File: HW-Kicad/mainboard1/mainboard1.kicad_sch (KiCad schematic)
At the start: 1 part, among them M1 LightAPRS

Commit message: comienzo mainboard
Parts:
- removed M1: LightAPRS, LightAPRS:LightAPRS, symbol LightAPRS:LightAPRS
- added J1: Conn_01x02_Male, Connector_Molex:Molex_KK-254_AE-6410-02A_1x02_P2.54mm_Vertical, symbol Connector:Conn_01x02_Male
- added J2: Conn_01x02_Male, Connector_PinHeader_2.54mm:PinHeader_1x02_P2.54mm_Horizontal, symbol Connector:Conn_01x02_Male
- added J3: Conn_01x07_Male, Connector_PinHeader_2.54mm:PinHeader_1x07_P2.54mm_Horizontal, symbol Connector:Conn_01x07_Male
- added J4, J5: Conn_01x04_Male, Connector_Molex:Molex_KK-254_AE-6410-04A_1x04_P2.54mm_Vertical, symbol Connector:Conn_01x04_Male
- added U1: ESP32-DevKitC, espressif:ESP32-DevKitC, symbol Espressif:ESP32-DevKitC
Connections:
- new net GND: J1.2 (Pin_2), J2.2 (Pin_2), J4.4 (Pin_4), J5.4 (Pin_4), U1.32 (GND), U1.38 (GND)
- new net MISO: J3.6 (Pin_6)
- new net MOSI: J3.7 (Pin_7)
- new net PAYLOAD1RX: J4.2 (Pin_2)
- new net PAYLOAD1TX: J4.3 (Pin_3)
- new net PAYLOAD2RX: J5.2 (Pin_2)
- new net PAYLOAD2TX: J5.3 (Pin_3)
- new net RST: J3.2 (Pin_2)
- new net SCK: J3.5 (Pin_5)
- new net SCL: J3.3 (Pin_3)
- new net SDA: J3.4 (Pin_4)
- new net VBAT: J1.1 (Pin_1), J2.1 (Pin_1), J4.1 (Pin_1), J5.1 (Pin_1), U1.19 (5V)
- no-connect marks 0 -> 1
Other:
- note added: "4,5 to 10v max"
- note added: "7.5V"
- note added: "Battery Module Input"
- note added: "LightAPRS Connector"
- note added: "Payload 1 Connector"
- note added: "Payload 2 Connector"

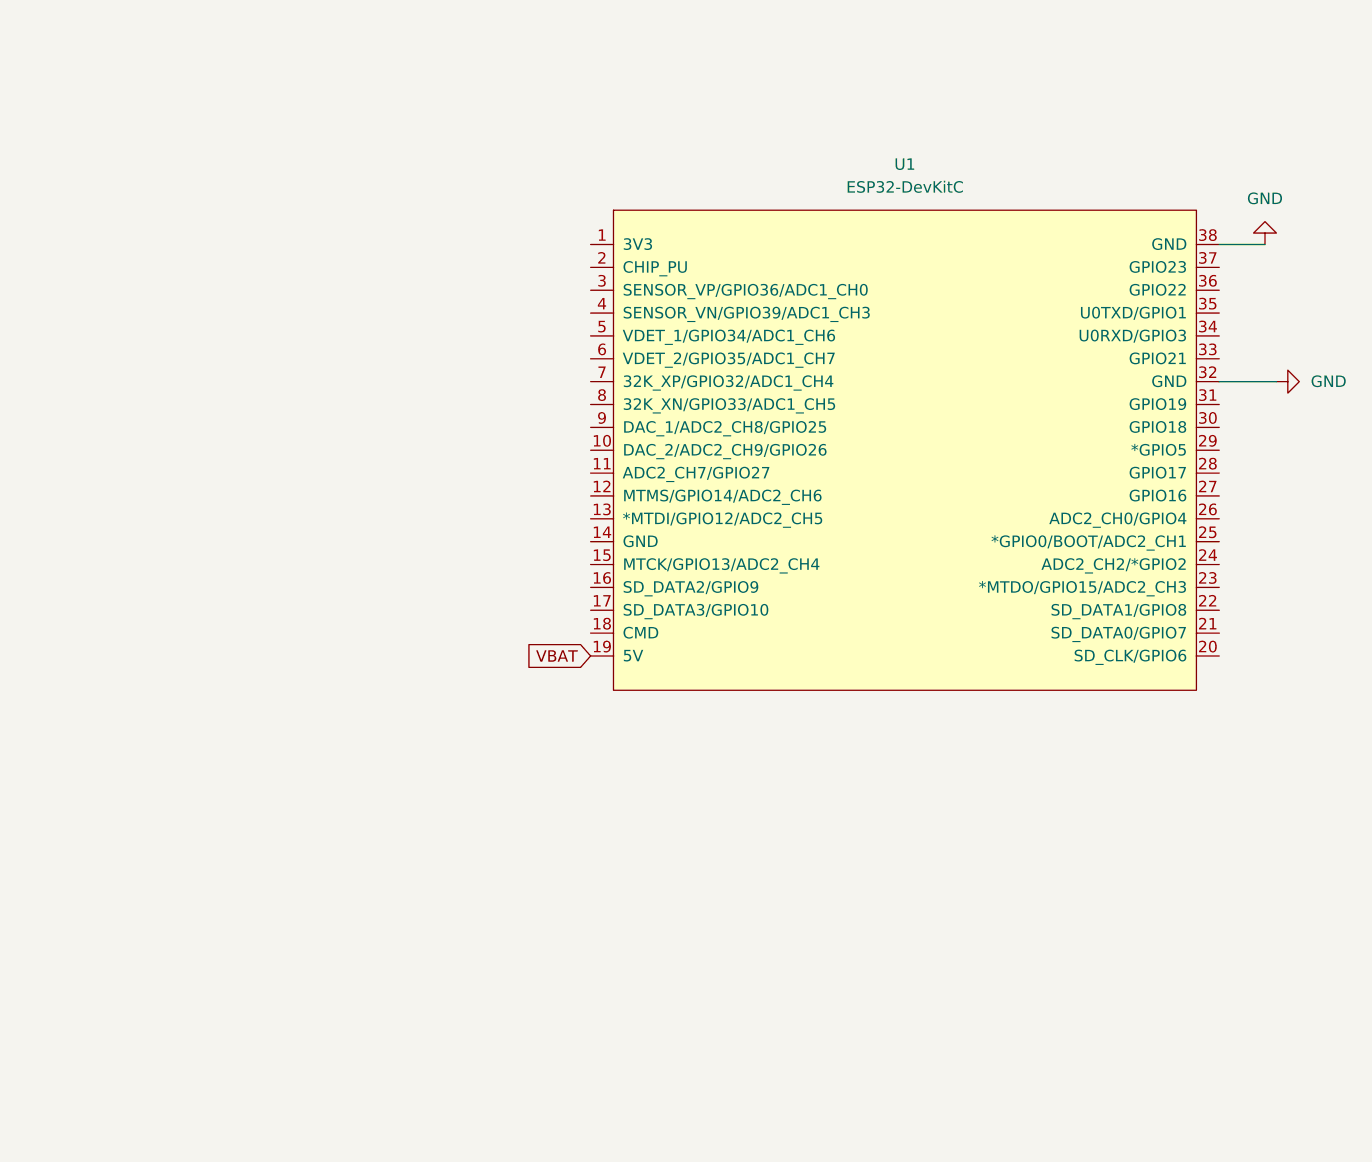
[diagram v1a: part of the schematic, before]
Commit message: cambio de footprint esp32 y ruteo de algunas pistas
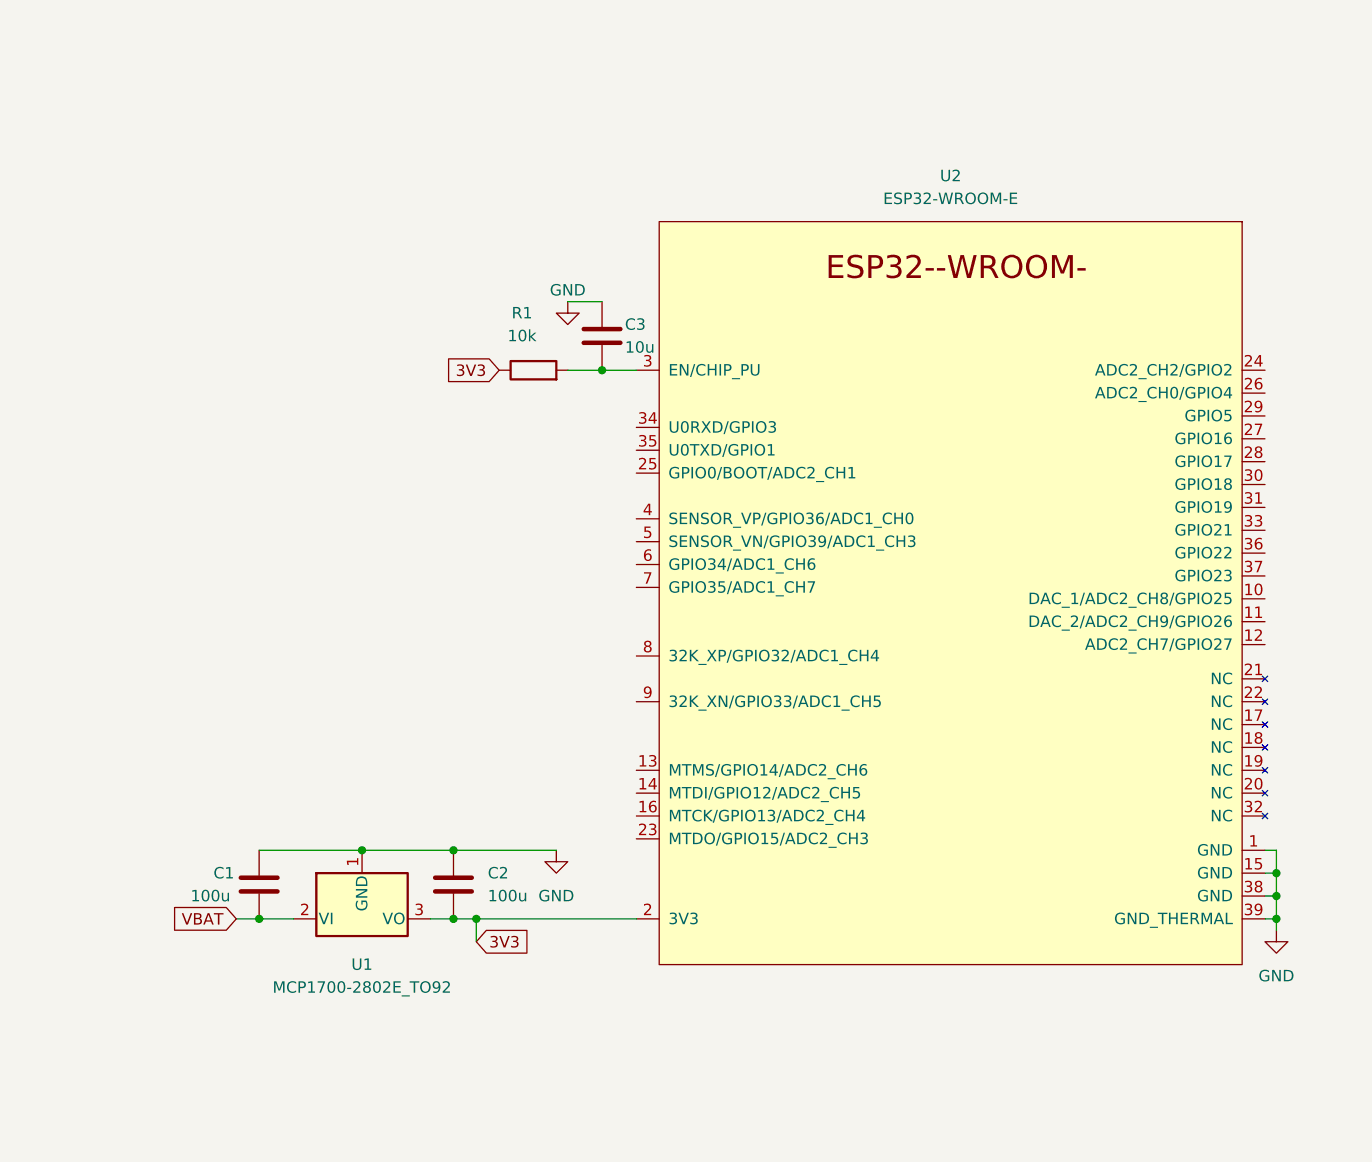
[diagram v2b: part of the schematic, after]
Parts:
- removed U1: ESP32-DevKitC, espressif:ESP32-DevKitC, symbol Espressif:ESP32-DevKitC
- added C1, C2: 100u, Capacitor_THT:CP_Radial_D6.3mm_P2.50mm, symbol Device:C
- added C3: 10u, Capacitor_THT:CP_Radial_D4.0mm_P2.00mm, symbol Device:C
- added R1: 10k, Resistor_THT:R_Axial_DIN0207_L6.3mm_D2.5mm_P7.62mm_Horizontal, symbol Device:R
- added U1: MCP1700-2802E_TO92, Package_TO_SOT_THT:TO-92_Inline, symbol Regulator_Linear:MCP1700-2802E_TO92
- added U2: ESP32-WROOM-E, ESP32:esp32_breakout, symbol Espressif:ESP32-WROOM-E
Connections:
- net GND: now also C1.1, C2.1, C3.1, U1.1 (GND), U2.1 (GND), U2.15 (GND), U2.38 (GND), U2.39 (GND_THERMAL)
- net VBAT: now also C1.2, U1.2 (VI)
- new net: C3.2, R1.2, U2.3 (EN/CHIP_PU)
- new net 3V3: C2.2, R1.1, U1.3 (VO), U2.2 (3V3)
